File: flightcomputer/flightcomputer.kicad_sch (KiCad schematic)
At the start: 75 parts, among them J1 Conn_Coaxial, J10 Conn_01x03, J11 Conn_01x03, J12 ESQ-113-14-G-D, J13 Conn_01x07, J14 S3B-PH-K-S-GW, J2 Conn_Coaxial, J3 Conn_Coaxial, J4 Conn_Coaxial, J5 S3B-PH-K-S-GW, J6 Conn_01x03, J7 S4B-PH-K-S_LF__SN_, J8 Conn_01x03, J9 Conn_01x06, U1 MAX-M10S, U2 LIS2MDLTR, U3 BMI088, U4 MS5607-02BA, U5 ESP32-S3-WROOM-1-N4, U6 S2P-VH, U7 Teensy4.1, U8 LSM6DSO32TR, U9 RFM96W-433S2

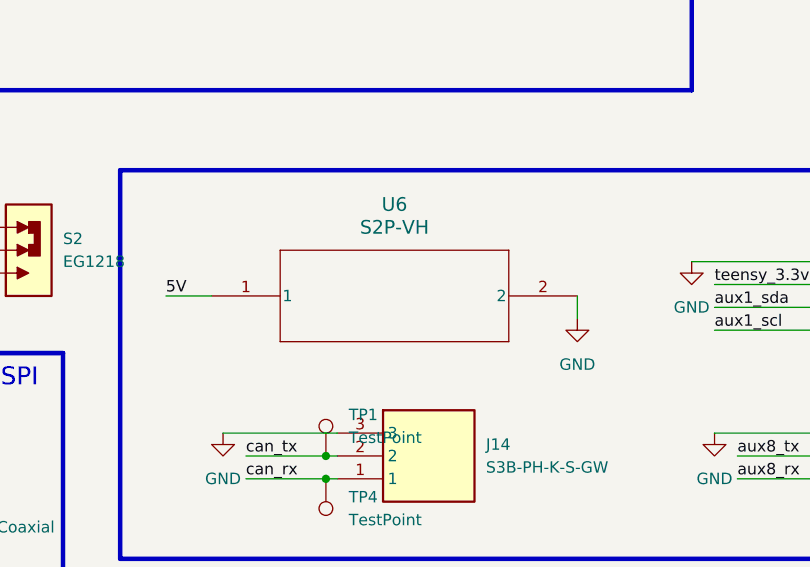
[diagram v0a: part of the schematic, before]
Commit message: use vert jst
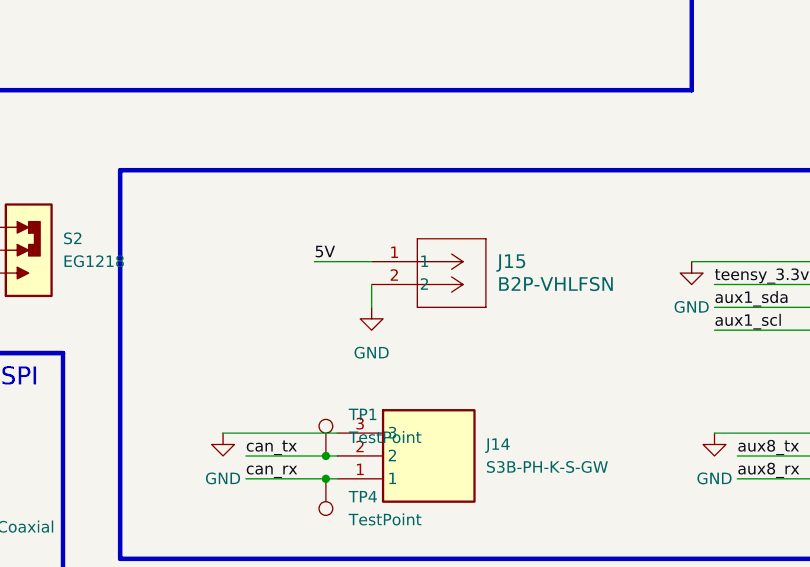
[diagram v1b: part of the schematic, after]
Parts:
- removed U6: S2P-VH, S2P-VH_JST, symbol HPRsymbols:S2P-VH
- added J15: B2P-VHLFSN, HPRlibrary:CONN_B2P-VH_JST, symbol HPRsymbols:B2P-VHLFSN
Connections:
- net 5V: now also J15.1
- net GND: now also J15.2
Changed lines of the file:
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@@
 	(wire
 		(pts
-			(xy 299.72 219.71) (xy 304.8 219.71)
+			(xy 316.23 215.9) (xy 322.58 215.9)
 		)
 		(stroke
@@
 	(wire
 		(pts
-			(xy 345.44 222.25) (xy 345.44 219.71)
+			(xy 322.58 220.98) (xy 322.58 218.44)
 		)
 		(stroke
@@
 	)
 	(label "5V"
-		(at 299.72 219.71 0)
+		(at 316.23 215.9 0)
 		(effects
 			(font
@@
 	(symbol
 		(lib_id "power:GND")
-		(at 345.44 222.25 0)
+		(at 322.58 220.98 0)
 		(unit 1)
 		(exclude_from_sim no)
@@
 		(fields_autoplaced yes)
 		(property "Reference" "#PWR033"
-			(at 345.44 228.6 0)
+			(at 322.58 227.33 0)
 			(effects
 				(font
@@
 		)
 		(property "Value" "GND"
-			(at 345.44 227.33 0)
+			(at 322.58 226.06 0)
 			(effects
 				(font
@@
 		)
 		(property "Footprint" ""
-			(at 345.44 222.25 0)
+			(at 322.58 220.98 0)
 			(effects
 				(font
@@
 		)
 		(property "Datasheet" ""
-			(at 345.44 222.25 0)
+			(at 322.58 220.98 0)
 			(effects
 				(font
@@
 		)
 		(property "Description" "Power symbol creates a global label with name \"GND\" , ground"
-			(at 345.44 222.25 0)
+			(at 322.58 220.98 0)
 			(effects
 				(font
@@
 	)
 	(symbol
-		(lib_id "HPRsymbols:S2P-VH")
-		(at 304.8 219.71 0)
-		(unit 1)
-		(exclude_from_sim no)
-		(in_bom yes)
-		(on_board yes)
-		(dnp no)
-		(fields_autoplaced yes)
-		(property "Reference" "U6"
-			(at 325.12 209.55 0)
-			(effects
-				(font
-					(size 1.524 1.524)
-				)
-			)
-		)
-		(property "Value" "S2P-VH"
-			(at 325.12 212.09 0)
-			(effects
-				(font
-					(size 1.524 1.524)
-				)
-			)
-		)
-		(property "Footprint" "S2P-VH_JST"
-			(at 304.8 219.71 0)
-			(effects
-				(font
-					(size 1.27 1.27)
-					(italic yes)
-				)
-				(hide yes)
-			)
-		)
-		(property "Datasheet" "S2P-VH"
-			(at 304.8 219.71 0)
-			(effects
-				(font
-					(size 1.27 1.27)
-					(italic yes)
-				)
-				(hide yes)
-			)
-		)
-		(property "Description" ""
-			(at 304.8 219.71 0)
-			(effects
-				(font
-					(size 1.27 1.27)
-				)
-				(hide yes)
-			)
-		)
-		(pin "2"
-		)
-		(pin "1"
-		)
-		(instances
-			(project ""
-				(path "/7ffad011-bb39-4f19-b4f2-0143f1626449"
-					(reference "U6")
-					(unit 1)
-				)
-			)
-		)
-	)
-	(symbol
 		(lib_id "HPRlibrary:S4B-PH-K-S_LF__SN_")
 		(at 373.38 215.9 0)
@@
 					(unit 1)
 				)
+			)
+		)
+	)
+	(symbol
+		(lib_id "HPRsymbols:B2P-VHLFSN")
+		(at 322.58 215.9 0)
+		(unit 1)
+		(exclude_from_sim no)
+		(in_bom yes)
+		(on_board yes)
+		(dnp no)
+		(property "Reference" "J15"
+			(at 336.55 215.8999 0)
+			(effects
+				(font
+					(size 1.524 1.524)
+				)
+				(justify left)
+			)
+		)
+		(property "Value" "B2P-VHLFSN"
+			(at 336.55 218.4399 0)
+			(effects
+				(font
+					(size 1.524 1.524)
+				)
+				(justify left)
+			)
+		)
+		(property "Footprint" "HPRlibrary:CONN_B2P-VH_JST"
+			(at 322.58 215.9 0)
+			(effects
+				(font
+					(size 1.27 1.27)
+					(italic yes)
+				)
+				(hide yes)
+			)
+		)
+		(property "Datasheet" "B2P-VHLFSN"
+			(at 322.58 215.9 0)
+			(effects
+				(font
+					(size 1.27 1.27)
+					(italic yes)
+				)
+				(hide yes)
+			)
+		)
+		(property "Description" ""
+			(at 322.58 215.9 0)
+			(effects
+				(font
+					(size 1.27 1.27)
+				)
+				(hide yes)
+			)
+		)
+		(pin "2"
+		)
+		(pin "1"
+		)
+		(instances
+			(project ""
+				(path "/7ffad011-bb39-4f19-b4f2-0143f1626449"
+					(reference "J15")
+					(unit 1)
+				)

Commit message: add LDO fc
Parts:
- added C11, C12: 1uF, Capacitor_SMD:C_0603_1608Metric_Pad1.08x0.95mm_HandSolder, symbol Device:C_Small
- added R16: 31.6k, Resistor_SMD:R_0603_1608Metric_Pad0.98x0.95mm_HandSolder, symbol Device:R_Small
- added R18: 10k, Resistor_SMD:R_0603_1608Metric_Pad0.98x0.95mm_HandSolder, symbol Device:R_Small
- added R19: 0, Resistor_SMD:R_0603_1608Metric_Pad0.98x0.95mm_HandSolder, symbol Device:R_Small
- added U6: NCP718ASNADJT1G, HPRlibrary:TSOT-23-5_2P9X1P6_ONS-L, symbol HPRsymbols:NCP718ASNADJT1G
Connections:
- net 5V: now also R19.2; no longer J15.1
- net GND: now also C11.2, C12.1, R18.2, U6.2 (GND)
- new net: R16.1, R18.1, U6.4 (NC/ADJ)
- new net LDO_5V: C12.2, R16.2, R19.1, U6.5 (OUT)
- new net V_ext: C11.1, J15.1, U6.1 (IN), U6.3 (EN)
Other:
- note added: "5V LDO"
- moved on the sheet: C1, C2, C3, C4, C5, C6, H1, H2, H3, H4, U2, U3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

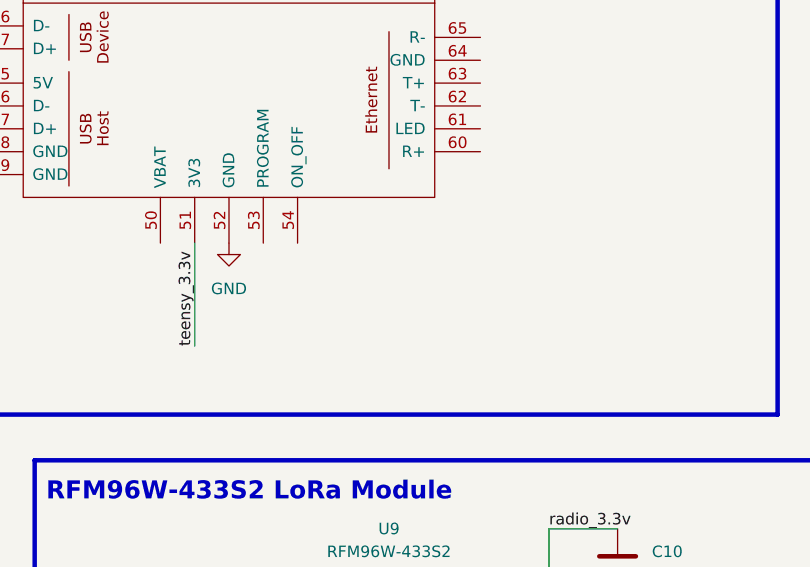
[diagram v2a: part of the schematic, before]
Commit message: add on/off test pad
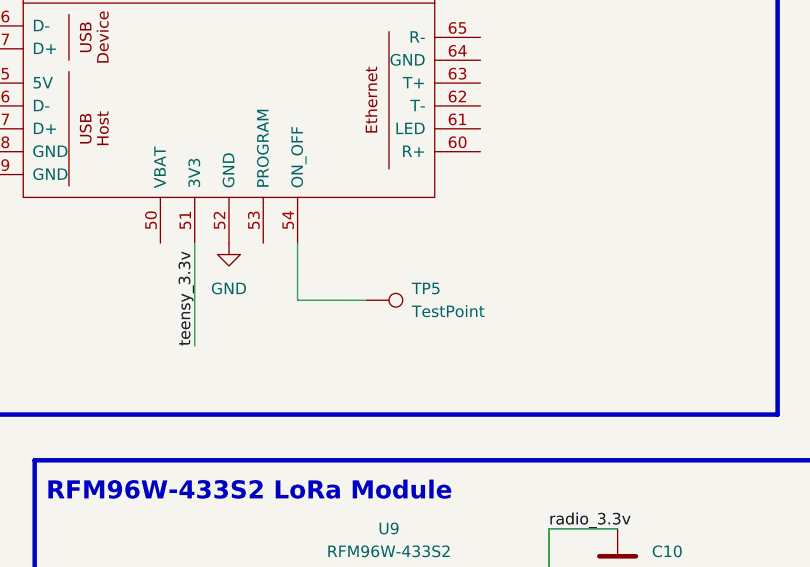
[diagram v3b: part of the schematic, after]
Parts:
- added TP5: TestPoint, TestPoint:TestPoint_Pad_D2.0mm, symbol Connector:TestPoint
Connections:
- net at U7.54 (ON_OFF): now also TP5.1
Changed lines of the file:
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@@
 	(wire
 		(pts
+			(xy 205.74 208.28) (xy 213.36 208.28)
+		)
+		(stroke
+			(width 0)
+			(type default)
+		)
+	)
+	(wire
+		(pts
 			(xy 86.36 138.43) (xy 86.36 137.16)
 		)
@@
 	(wire
 		(pts
+			(xy 205.74 201.93) (xy 205.74 208.28)
+		)
+		(stroke
+			(width 0)
+			(type default)
+		)
+	)
+	(wire
+		(pts
 			(xy 233.68 233.68) (xy 233.68 241.3)
 		)
@@
 					(unit 1)
 				)
+			)
+		)
+	)
+	(symbol
+		(lib_id "Connector:TestPoint")
+		(at 213.36 208.28 270)
+		(unit 1)
+		(exclude_from_sim no)
+		(in_bom yes)
+		(on_board yes)
+		(dnp no)
+		(fields_autoplaced yes)
+		(property "Reference" "TP5"
+			(at 218.44 207.0099 90)
+			(effects
+				(font
+					(size 1.27 1.27)
+				)
+				(justify left)
+			)
+		)
+		(property "Value" "TestPoint"
+			(at 218.44 209.5499 90)
+			(effects
+				(font
+					(size 1.27 1.27)
+				)
+				(justify left)
+			)
+		)
+		(property "Footprint" "TestPoint:TestPoint_Pad_D2.0mm"
+			(at 213.36 213.36 0)
+			(effects
+				(font
+					(size 1.27 1.27)
+				)
+				(hide yes)
+			)
+		)
+		(property "Datasheet" "~"
+			(at 213.36 213.36 0)
+			(effects
+				(font
+					(size 1.27 1.27)
+				)
+				(hide yes)
+			)
+		)
+		(property "Description" "test point"
+			(at 213.36 208.28 0)
+			(effects
+				(font
+					(size 1.27 1.27)
+				)
+				(hide yes)
+			)
+		)
+		(pin "1"
+		)
+		(instances
+			(project ""
+				(path "/7ffad011-bb39-4f19-b4f2-0143f1626449"
+					(reference "TP5")
+					(unit 1)
+				)

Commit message: prod files
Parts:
- added R20: 0, Resistor_SMD:R_0603_1608Metric_Pad0.98x0.95mm_HandSolder, symbol Device:R_Small
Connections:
- net radio_3.3v: now also R20.2
- net teensy_3.3v: now also R20.1
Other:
- moved on the sheet: S2
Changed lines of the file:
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@@
 	)
 	(rectangle
-		(start 294.64 205.74)
+		(start 301.625 205.74)
 		(end 405.13 248.92)
 		(stroke
@@
 	(wire
 		(pts
-			(xy 266.7 217.17) (xy 279.4 217.17)
+			(xy 276.86 217.17) (xy 288.29 217.17)
 		)
 		(stroke
@@
 	(wire
 		(pts
+			(xy 264.16 220.98) (xy 267.97 220.98)
+		)
+		(stroke
+			(width 0)
+			(type default)
+		)
+	)
+	(wire
+		(pts
 			(xy 157.48 139.7) (xy 170.18 139.7)
 		)
@@
 	(wire
 		(pts
+			(xy 264.16 217.17) (xy 264.16 220.98)
+		)
+		(stroke
+			(width 0)
+			(type default)
+		)
+	)
+	(wire
+		(pts
 			(xy 226.06 152.4) (xy 240.03 152.4)
 		)
@@
 	(wire
 		(pts
+			(xy 264.16 208.28) (xy 267.97 208.28)
+		)
+		(stroke
+			(width 0)
+			(type default)
+		)
+	)
+	(wire
+		(pts
 			(xy 105.41 213.36) (xy 118.11 213.36)
 		)
@@
 	(wire
 		(pts
+			(xy 264.16 212.09) (xy 264.16 208.28)
+		)
+		(stroke
+			(width 0)
+			(type default)
+		)
+	)
+	(wire
+		(pts
 			(xy 226.06 124.46) (xy 240.03 124.46)
 		)
@@
 	(wire
 		(pts
-			(xy 266.7 214.63) (xy 279.4 214.63)
+			(xy 276.86 214.63) (xy 288.29 214.63)
 		)
 		(stroke
@@
 		)
 	)
+	(label "teensy_3.3v"
+		(at 267.97 208.28 0)
+		(effects
+			(font
+				(size 1.27 1.27)
+			)
+			(justify left bottom)
+		)
+	)
 	(label "GPS_int"
 		(at 240.03 127 180)
@@
 		)
 	)
+	(label "radio_3.3v"
+		(at 267.97 220.98 0)
+		(effects
+			(font
+				(size 1.27 1.27)
+			)
+			(justify left bottom)
+		)
+	)
 	(label "aux1_scl"
 		(at 231.14 139.7 0)
@@
 	)
 	(label "teensy_3.3v"
-		(at 266.7 214.63 0)
+		(at 276.86 214.63 0)
 		(effects
 			(font
@@
 	)
 	(label "radio_3.3v"
-		(at 266.7 217.17 0)
+		(at 276.86 217.17 0)
 		(effects
 			(font
@@
 	(symbol
 		(lib_id "HPRlibrary:EG1218")
-		(at 284.48 214.63 0)
+		(at 293.37 214.63 0)
 		(unit 1)
 		(exclude_from_sim no)
@@
 		(fields_autoplaced yes)
 		(property "Reference" "S2"
-			(at 288.29 213.3599 0)
+			(at 297.18 213.3599 0)
 			(effects
 				(font
@@
 		)
 		(property "Value" "EG1218"
-			(at 288.29 215.8999 0)
+			(at 297.18 215.8999 0)
 			(effects
 				(font
@@
 		)
 		(property "Footprint" "HPRlibrary:SW_EG1218"
-			(at 284.48 214.63 0)
+			(at 293.37 214.63 0)
 			(effects
 				(font
@@
 		)
 		(property "Datasheet" ""
-			(at 284.48 214.63 0)
+			(at 293.37 214.63 0)
 			(effects
 				(font
@@
 		)
 		(property "Description" "Slide Switch SPDT Through Hole"
-			(at 284.48 214.63 0)
+			(at 293.37 214.63 0)
 			(effects
 				(font
@@
 		)
 		(property "MF" "E-Switch"
-			(at 284.48 214.63 0)
+			(at 293.37 214.63 0)
 			(effects
 				(font
@@
 		)
 		(property "PACKAGE" "None"
-			(at 284.48 214.63 0)
+			(at 293.37 214.63 0)
 			(effects
 				(font
@@
 		)
 		(property "PRICE" "None"
-			(at 284.48 214.63 0)
+			(at 293.37 214.63 0)
 			(effects
 				(font
@@
 		)
 		(property "MP" "EG1218"
-			(at 284.48 214.63 0)
+			(at 293.37 214.63 0)
 			(effects
 				(font
@@
 		)
 		(property "AVAILABILITY" "In Stock"
-			(at 284.48 214.63 0)
+			(at 293.37 214.63 0)
 			(effects
 				(font
@@
 		)
 		(property "PURCHASE-URL" "https://pricing.snapeda.com/search/part/EG1218/?ref=eda"
-			(at 284.48 214.63 0)
+			(at 293.37 214.63 0)
 			(effects
 				(font
@@
 					(unit 1)
 				)
+			)
+		)
+	)
+	(symbol
+		(lib_id "Device:R_Small")
+		(at 264.16 214.63 0)
+		(unit 1)
+		(exclude_from_sim no)
+		(in_bom yes)
+		(on_board yes)
+		(dnp yes)
+		(fields_autoplaced yes)
+		(property "Reference" "R20"
+			(at 266.7 213.3599 0)
+			(effects
+				(font
+					(size 1.016 1.016)
+				)
+				(justify left)
+			)
+		)
+		(property "Value" "0"
+			(at 266.7 215.8999 0)
+			(effects
+				(font
+					(size 1.27 1.27)
+				)
+				(justify left)
+			)
+		)
+		(property "Footprint" "Resistor_SMD:R_0603_1608Metric_Pad0.98x0.95mm_HandSolder"
+			(at 264.16 214.63 0)
+			(effects
+				(font
+					(size 1.27 1.27)
+				)
+				(hide yes)
+			)
+		)
+		(property "Datasheet" "~"
+			(at 264.16 214.63 0)
+			(effects
+				(font
+					(size 1.27 1.27)
+				)
+				(hide yes)
+			)
+		)
+		(property "Description" "Resistor, small symbol"
+			(at 264.16 214.63 0)
+			(effects
+				(font
+					(size 1.27 1.27)
+				)
+				(hide yes)
+			)
+		)
+		(pin "1"
+		)
+		(pin "2"
+		)
+		(instances
+			(project ""
+				(path "/7ffad011-bb39-4f19-b4f2-0143f1626449"
+					(reference "R20")
+					(unit 1)
+				)
